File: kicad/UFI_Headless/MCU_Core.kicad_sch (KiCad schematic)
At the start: 46 parts, among them J4 SWD, J5 DBG_UART, SW1 RESET, SW2 BOOT, U11 APS6404L-3SQR-SN, U5 STM32H723ZGT6, Y1 25MHz CL=12pF

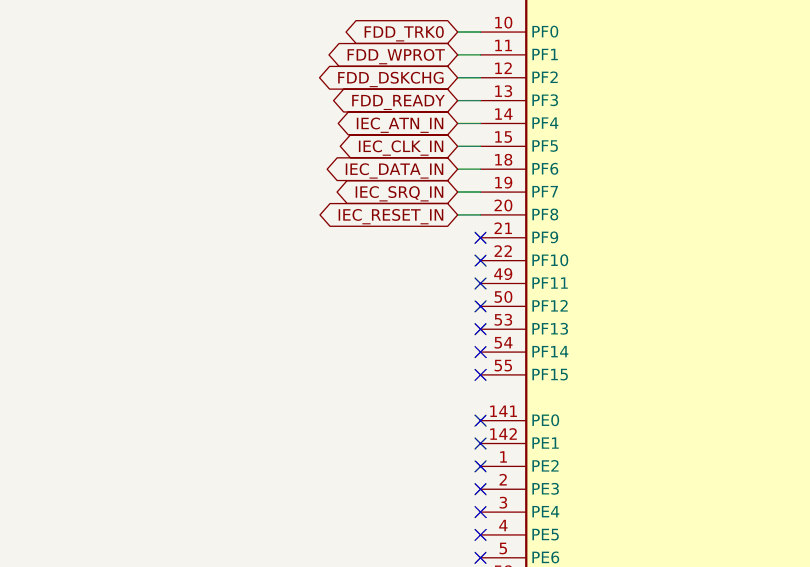
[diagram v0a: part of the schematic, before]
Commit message: UFI Headless v0.4: J6 pin 6 DRATE via JP1, pin 3 GND/+5V via JP2
DRATE is driven by PF11 through the spare LS07 gate U7.11 -> U7.10 with
pull-up RN3.3; J6 pin 6 only sees it when solder jumper JP1 is bridged.
J6 pin 3 goes through JP2 (default 1-2 = GND, 2-3 = FDD_5V for PS/2 drives).
Firmware moves FDD_DRATE from PE6 to PF11.
DRC 0 violations, 0 unconnected, parity clean; fab outputs regenerated.
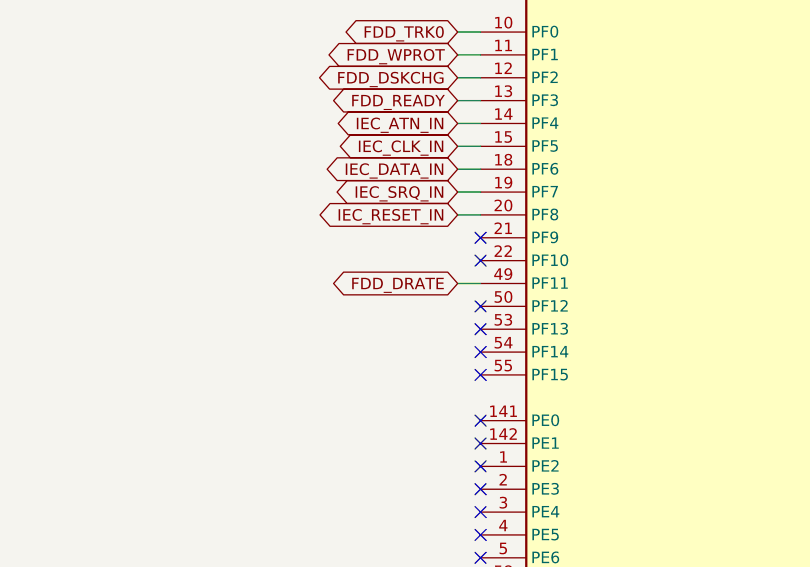
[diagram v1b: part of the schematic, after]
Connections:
- net FDD_DRATE: now reaches U5.49 (PF11)
- no-connect marks 67 -> 66

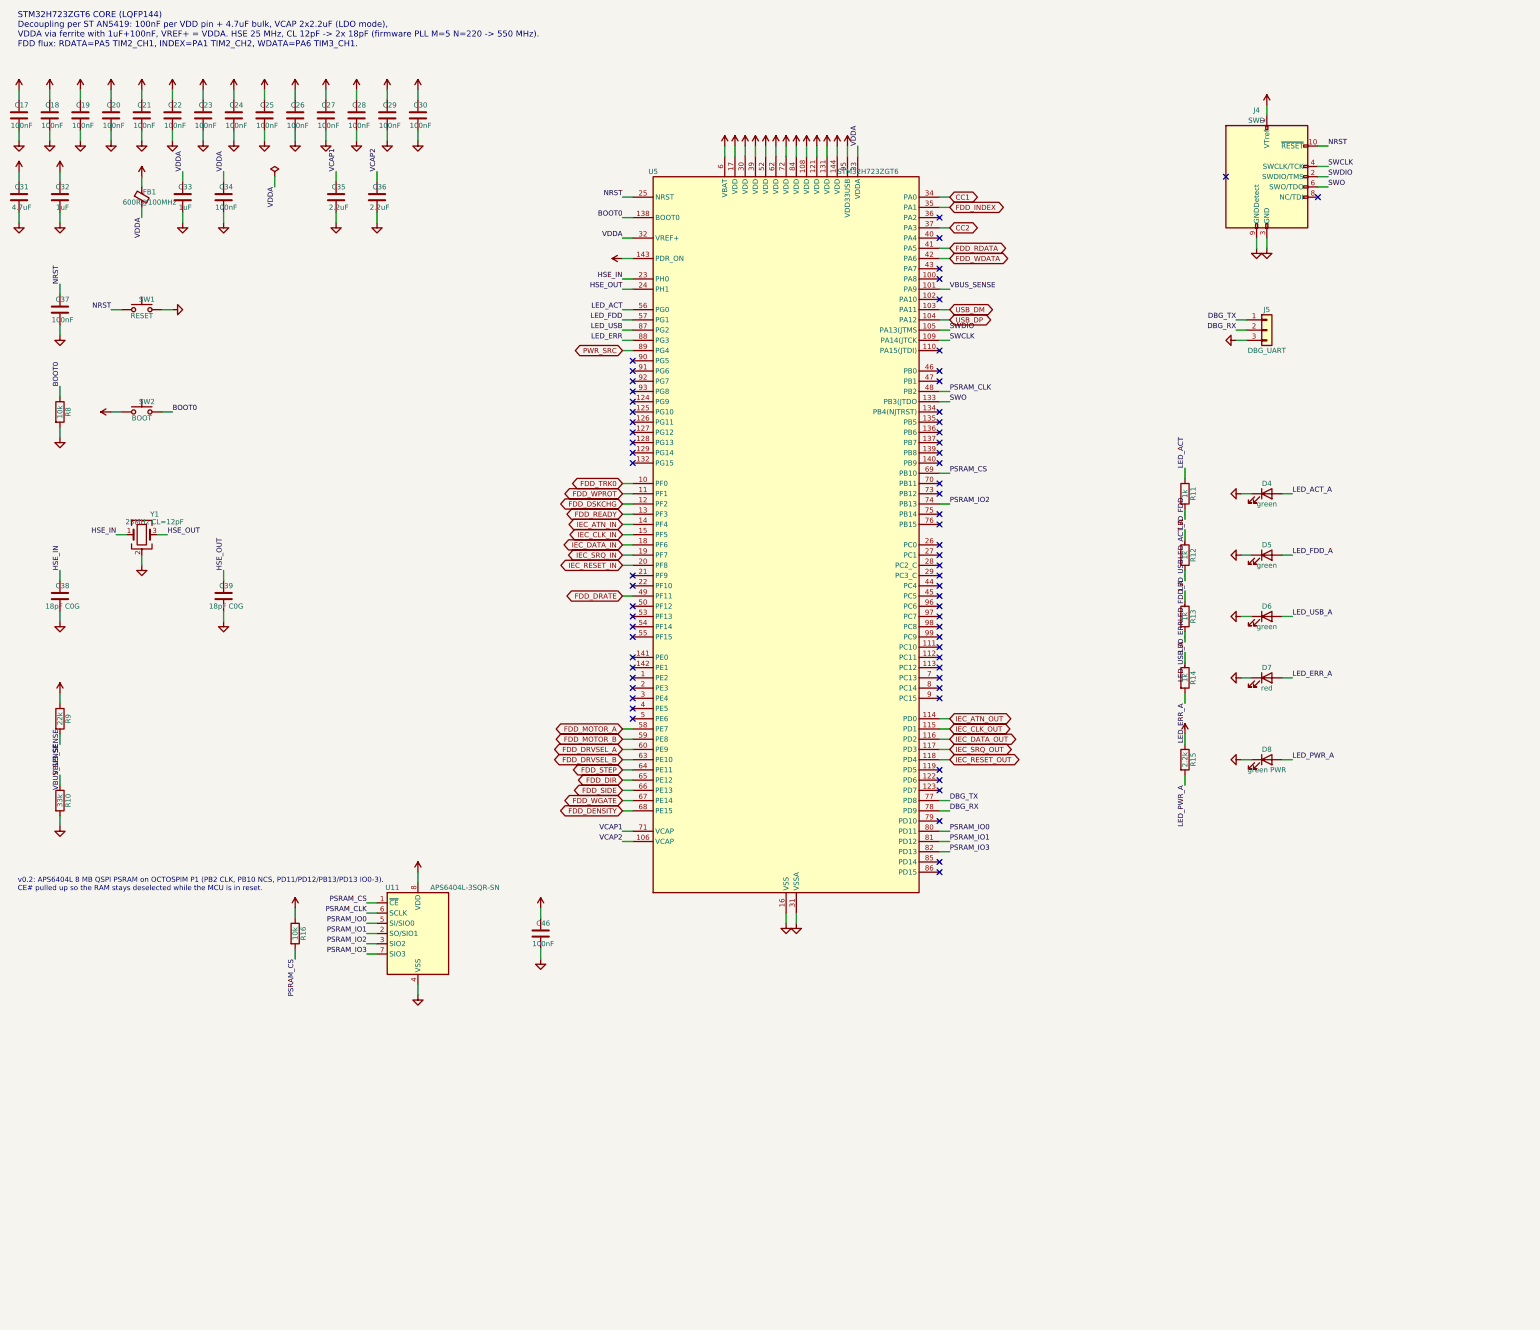
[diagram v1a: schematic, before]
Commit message: UFI Headless v0.5: switched/measured drive supplies, write lock, microSD, expansion
Hardware (A1-A9): FDD_5V/FDD_12V high-side P-FET switches (off in reset)
with 0.1R + INA180A1 current sense, TVS at both outputs; WRITE LOCK
jumper J11 gates WGATE through 74LVC1G32 (TP8 now shows the gated
signal); expansion header J9 (I2C1, 2 GPIO, button lines, 3V3/5V),
buttons SW3/SW4; microSD J10 on SDMMC2 with the card slot facing the
top edge; board ID divider on PA4; test points TP7/TP8.  12V reverse
protection already existed; 8-inch 50-pin port left out (board size).
ECO placed 37 parts; Freerouting plus hand routes for the rest.
New scripts/eco/ tools (maze router, route check, cluster/occupancy
maps, via scan), add_silk_label.py no longer crashes on re-placement.
ERC 0, DRC 0 incl. warnings, 0 unconnected, parity clean, no via-in-pad;
fab outputs regenerated (146 CPL rows).
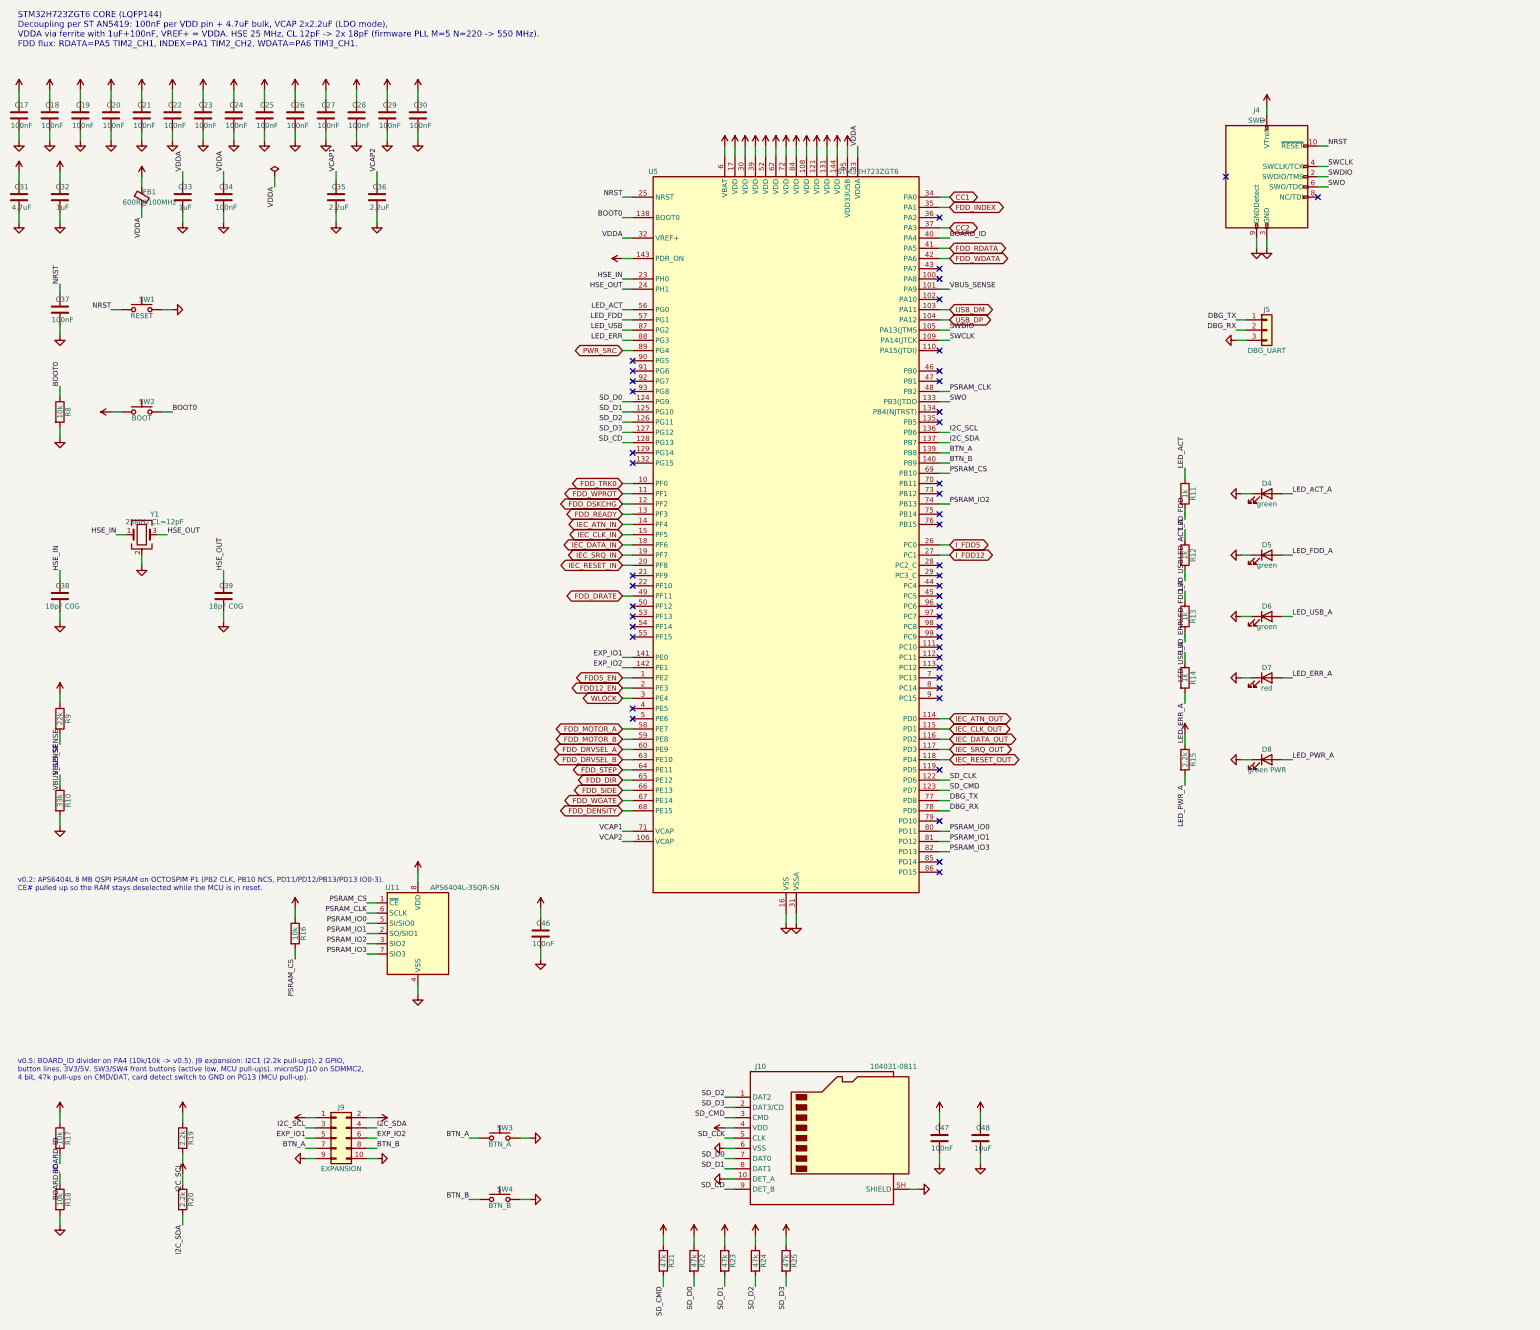
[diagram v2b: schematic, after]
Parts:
- added C47: 100nF, Capacitor_SMD:C_0603_1608Metric, symbol Device:C
- added C48: 10uF, Capacitor_SMD:C_0805_2012Metric, symbol Device:C
- added J10: 104031-0811, Connector_Card:microSD_HC_Molex_104031-0811, symbol Connector:Micro_SD_Card_Det2
- added J9: EXPANSION, Connector_PinHeader_2.54mm:PinHeader_2x05_P2.54mm_Vertical, symbol Connector_Generic:Conn_02x05_Odd_Even
- added R17, R18: 10k, Resistor_SMD:R_0603_1608Metric, symbol Device:R
- added R19, R20: 2.2k, Resistor_SMD:R_0603_1608Metric, symbol Device:R
- added R21, R22, R23, R24, R25: 47k, Resistor_SMD:R_0603_1608Metric, symbol Device:R
- added SW3: BTN_A, Button_Switch_SMD:SW_SPST_TL3342, symbol Switch:SW_Push
- added SW4: BTN_B, Button_Switch_SMD:SW_SPST_TL3342, symbol Switch:SW_Push
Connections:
- net +3V3: now also C47.1, C48.1, J10.4 (VDD), J9.1 (Pin_1), R17.1, R19.1, R20.1, R21.1, R22.1, R23.1, R24.1, R25.1
- net GND: now also C47.2, C48.2, J10.10 (DET_A), J10.6 (VSS), J10.SH (SHIELD), J9.10 (Pin_10), J9.9 (Pin_9), R18.2, SW3.2, SW4.2
- net FDD5_EN: now reaches U5.1 (PE2)
- net SD_CLK: now reaches U5.122 (PD6)
- net SD_CLK: now also J10.5 (CLK)
- net SD_CMD: now reaches U5.123 (PD7)
- net SD_CMD: now also J10.3 (CMD), R21.2
- net SD_D0: now reaches U5.124 (PG9)
- net SD_D0: now also J10.7 (DAT0), R22.2
- net SD_D1: now reaches U5.125 (PG10)
- net SD_D1: now also J10.8 (DAT1), R23.2
- net SD_D2: now reaches U5.126 (PG11)
- net SD_D2: now also J10.1 (DAT2), R24.2
- net SD_D3: now reaches U5.127 (PG12)
- net SD_D3: now also J10.2 (DAT3/CD), R25.2
- net SD_CD: now reaches U5.128 (PG13)
- net SD_CD: now also J10.9 (DET_B)
- net I2C_SCL: now reaches U5.136 (PB6)
- net I2C_SCL: now also J9.3 (Pin_3), R19.2
- net I2C_SDA: now reaches U5.137 (PB7)
- net I2C_SDA: now also J9.4 (Pin_4), R20.2
- net BTN_A: now reaches U5.139 (PB8)
- net BTN_A: now also J9.7 (Pin_7), SW3.1
- net BTN_B: now reaches U5.140 (PB9)
- net BTN_B: now also J9.8 (Pin_8), SW4.1
- net EXP_IO1: now reaches U5.141 (PE0)
- net EXP_IO1: now also J9.5 (Pin_5)
- net EXP_IO2: now reaches U5.142 (PE1)
- net EXP_IO2: now also J9.6 (Pin_6)
- net FDD12_EN: now reaches U5.2 (PE3)
- net I_FDD5: now reaches U5.26 (PC0)
- net I_FDD12: now reaches U5.27 (PC1)
- net WLOCK: now reaches U5.3 (PE4)
- net BOARD_ID: now reaches U5.40 (PA4)
- net BOARD_ID: now also R17.2, R18.1
- new net +5V: J9.2 (Pin_2)
- no-connect marks 66 -> 47
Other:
- note added: "v0.5: BOARD_ID divider on PA4 (10k/10k -> v0.5). J9 expansion: I2C1 (2.2k pull-ups), 2 GPIO, button lines, 3V3/5V. SW3/SW4 front buttons (active low, MCU pull-ups). microSD J10 on SDMMC2, 4 bit, 47k pull-ups on CMD/DAT, card detect switch to GND on PG13 (MCU pull-up)."

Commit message: v0.6: soldered SD NAND replaces the microSD slot; stand-alone dump + USB drive mode
Board (closed enclosure, no card access):
- J10 microSD removed; U15 SD NAND CSNP32GCR01-AOW (4 GB, C2841139) on the same
  SDMMC2 lines, project footprint fits MKDV8GIL-AST (1 GB) as well
- PG13 card detect dropped; board ID R18 4.7k (1055 mV = v0.6)
- project symbol/footprint library lib/, kisch.py + add_parts.py look there first
- ECO re-route; ERC 0, DRC 0 incl. warnings, 0 unconnected, parity clean, no via-in-pad
- new eco tools remove_part.py, set_value.py; fab outputs regenerated

Firmware 1.3:
- ufi_sd.c: block access + FatFs R0.12c disk glue (Cube middleware, ffconf.h)
- ufi_dump.c: button A >= 1 s / DUMP_START dumps the disk to DUMPnnnn.SCP,
  byte-identical to `ufi read-disk` (host simulation, 5 configurations);
  button B aborts, ERR blink codes
- USB mass storage mode (ST MSC class, ufi_msc.c): button B >= 2 s or USB_MSC
- commands 0x50-0x53, error code 13 (storage), GET_INFO knows v0.6
- CI: FatFs added to the sparse STM32CubeH7 checkout

Docs: READMEs, ordering guide (part cost, 1 GB alternative), bring-up checklist.
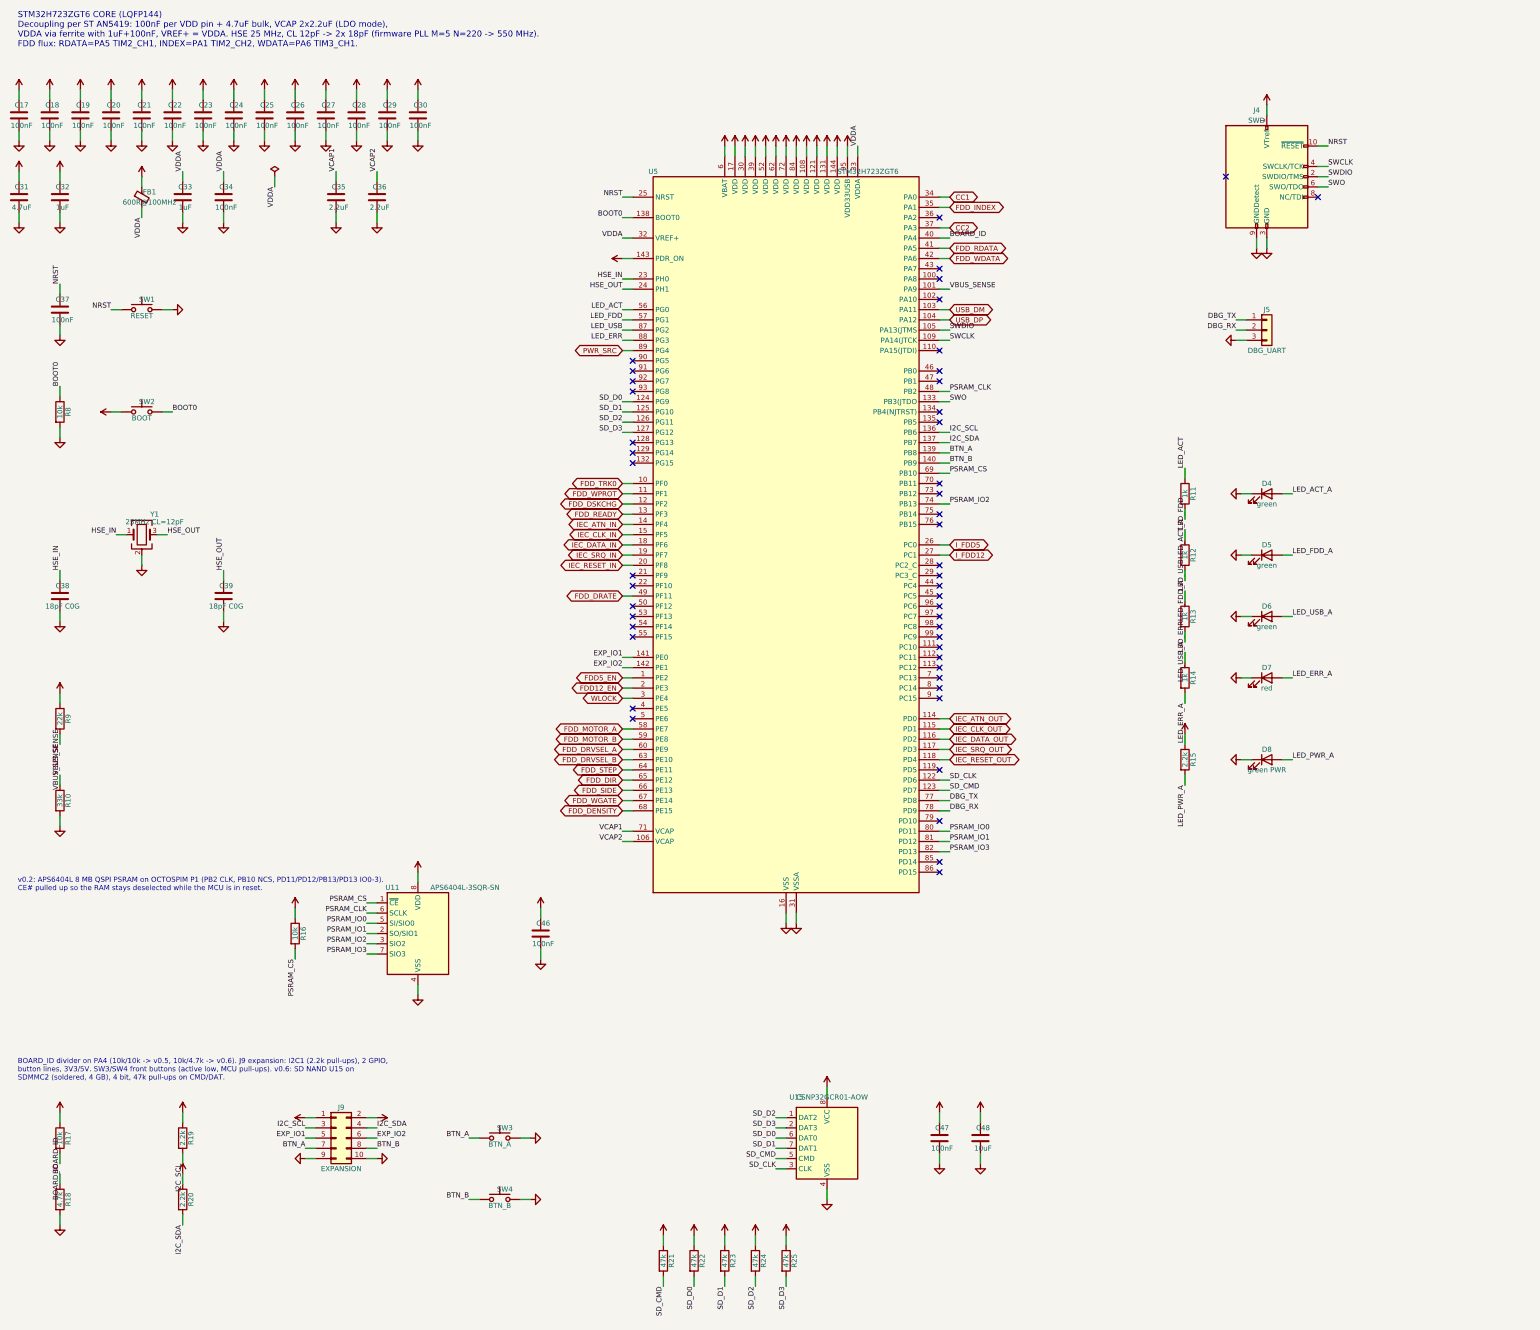
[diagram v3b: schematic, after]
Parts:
- removed J10: 104031-0811, Connector_Card:microSD_HC_Molex_104031-0811, symbol Connector:Micro_SD_Card_Det2
- added U15: CSNP32GCR01-AOW, UFI_Headless:SD_NAND_LGA-8_6x8mm_P1.27mm, symbol UFI_Headless:SD_NAND_LGA8
- R18: value 10k -> 4.7k; LCSC C25804 -> C23162
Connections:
- net +3V3: now also U15.8 (VCC)
- net GND: now also U15.4 (VSS)
- net SD_CLK: now also U15.3 (CLK)
- net SD_CMD: now also U15.5 (CMD)
- net SD_D0: now also U15.6 (DAT0)
- net SD_D1: now also U15.7 (DAT1)
- net SD_D2: now also U15.1 (DAT2)
- net SD_D3: now also U15.2 (DAT3)
- net SD_CD: no longer names the net of U5.128 (PG13)
- no-connect marks 47 -> 48
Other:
- note added: "BOARD_ID divider on PA4 (10k/10k -> v0.5, 10k/4.7k -> v0.6). J9 expansion: I2C1 (2.2k pull-ups), 2 GPIO, button lines, 3V3/5V. SW3/SW4 front buttons (active low, MCU pull-ups). v0.6: SD NAND U15 on SDMMC2 (soldered, 4 GB), 4 bit, 47k pull-ups on CMD/DAT."
- note removed: "v0.5: BOARD_ID divider on PA4 (10k/10k -> v0.5). J9 expansion: I2C1 (2.2k pull-ups), 2 GPIO, button lines, 3V3/5V. SW3/SW4 front buttons (active low, MCU pull-ups). microSD J10 on SDMMC2, 4 bit, 47k pull-ups on CMD/DAT, card detect switch to GND on PG13 (MCU pull-up)."
